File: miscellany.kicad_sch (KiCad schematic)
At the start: 12 parts, among them U3 74HC112, U5 74HC123

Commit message: additional PCB cleanup
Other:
- moved on the sheet: C2, C3, C4, C5, C6, C8, H1, H2, H3, H4

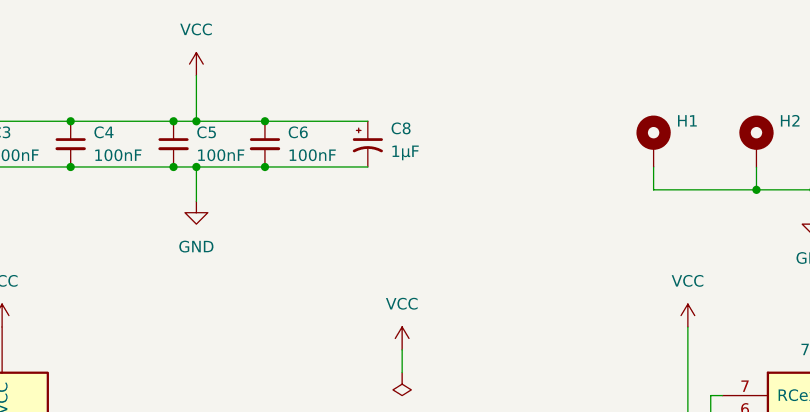
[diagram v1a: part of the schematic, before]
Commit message: reset schematic annotations
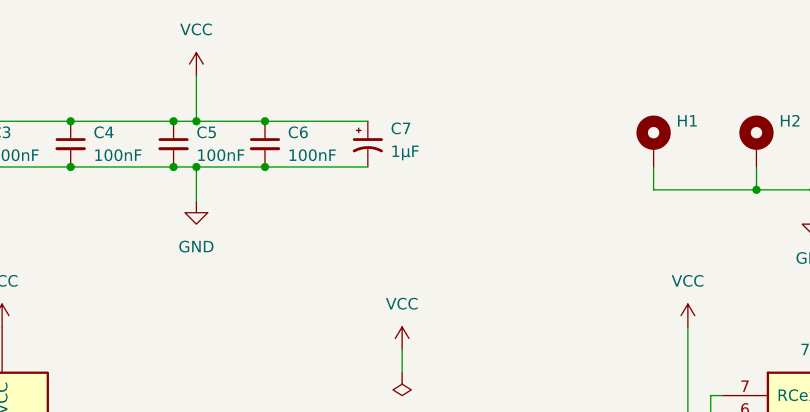
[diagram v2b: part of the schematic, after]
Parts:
- renumbered C8 to C7
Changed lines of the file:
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@@
 		(dnp no)
 		(fields_autoplaced yes)
-		(property "Reference" "#PWR016"
+		(property "Reference" "#PWR019"
 			(at 48.26 173.99 0)
 			(effects
@@
 			(project "am9511-6502"
 				(path "/492d2c5d-68ab-43c4-8db3-0d52dc374f84/1253bf53-8160-4ac9-adc0-ad2136e38890"
-					(reference "#PWR016")
+					(reference "#PWR019")
 					(unit 1)
 				)
@@
 		(dnp no)
 		(fields_autoplaced yes)
-		(property "Reference" "#PWR019"
+		(property "Reference" "#PWR023"
 			(at 92.71 176.53 0)
 			(effects
@@
 			(project "am9511-6502"
 				(path "/492d2c5d-68ab-43c4-8db3-0d52dc374f84/1253bf53-8160-4ac9-adc0-ad2136e38890"
-					(reference "#PWR019")
+					(reference "#PWR023")
 					(unit 1)
 				)
@@
 		(dnp no)
 		(fields_autoplaced yes)
-		(property "Reference" "#PWR026"
+		(property "Reference" "#PWR027"
 			(at 138.43 163.83 0)
 			(effects
@@
 			(project ""
 				(path "/492d2c5d-68ab-43c4-8db3-0d52dc374f84/1253bf53-8160-4ac9-adc0-ad2136e38890"
-					(reference "#PWR026")
+					(reference "#PWR027")
 					(unit 1)
 				)
@@
 		(dnp no)
 		(fields_autoplaced yes)
-		(property "Reference" "C8"
+		(property "Reference" "C7"
 			(at 91.44 148.1581 0)
 			(effects
@@
 			(project ""
 				(path "/492d2c5d-68ab-43c4-8db3-0d52dc374f84/1253bf53-8160-4ac9-adc0-ad2136e38890"
-					(reference "C8")
+					(reference "C7")
 					(unit 1)
 				)
@@
 		(dnp no)
 		(fields_autoplaced yes)
-		(property "Reference" "#PWR020"
+		(property "Reference" "#PWR024"
 			(at 92.71 198.12 0)
 			(effects
@@
 			(project "am9511-6502"
 				(path "/492d2c5d-68ab-43c4-8db3-0d52dc374f84/1253bf53-8160-4ac9-adc0-ad2136e38890"
-					(reference "#PWR020")
+					(reference "#PWR024")
 					(unit 1)
 				)
@@
 		(dnp no)
 		(fields_autoplaced yes)
-		(property "Reference" "#PWR014"
+		(property "Reference" "#PWR017"
 			(at 24.13 173.99 0)
 			(effects
@@
 			(project "am9511-6502"
 				(path "/492d2c5d-68ab-43c4-8db3-0d52dc374f84/1253bf53-8160-4ac9-adc0-ad2136e38890"
-					(reference "#PWR014")
+					(reference "#PWR017")
 					(unit 1)
 				)
@@
 		(dnp no)
 		(fields_autoplaced yes)
-		(property "Reference" "#PWR015"
+		(property "Reference" "#PWR018"
 			(at 24.13 201.93 0)
 			(effects
@@
 			(project "am9511-6502"
 				(path "/492d2c5d-68ab-43c4-8db3-0d52dc374f84/1253bf53-8160-4ac9-adc0-ad2136e38890"
-					(reference "#PWR015")
+					(reference "#PWR018")
 					(unit 1)
 				)
@@
 		(dnp no)
 		(fields_autoplaced yes)
-		(property "Reference" "#PWR017"
+		(property "Reference" "#PWR020"
 			(at 48.26 201.93 0)
 			(effects
@@
 			(project "am9511-6502"
 				(path "/492d2c5d-68ab-43c4-8db3-0d52dc374f84/1253bf53-8160-4ac9-adc0-ad2136e38890"
-					(reference "#PWR017")
+					(reference "#PWR020")
 					(unit 1)
 				)
@@
 		(dnp no)
 		(fields_autoplaced yes)
-		(property "Reference" "#PWR018"
+		(property "Reference" "#PWR025"
 			(at 124.46 173.99 0)
 			(effects
@@
 			(project "am9511-6502"
 				(path "/492d2c5d-68ab-43c4-8db3-0d52dc374f84/1253bf53-8160-4ac9-adc0-ad2136e38890"
-					(reference "#PWR018")
+					(reference "#PWR025")
 					(unit 1)
 				)
@@
 		(dnp no)
 		(fields_autoplaced yes)
-		(property "Reference" "#PWR028"
+		(property "Reference" "#PWR026"
 			(at 127 198.12 0)
 			(effects
@@
 			(project ""
 				(path "/492d2c5d-68ab-43c4-8db3-0d52dc374f84/1253bf53-8160-4ac9-adc0-ad2136e38890"
-					(reference "#PWR028")
-					(unit 1)
-				)
+					(reference "#PWR026")
+					(unit 1)
+				)
